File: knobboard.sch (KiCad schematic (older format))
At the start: 0 parts

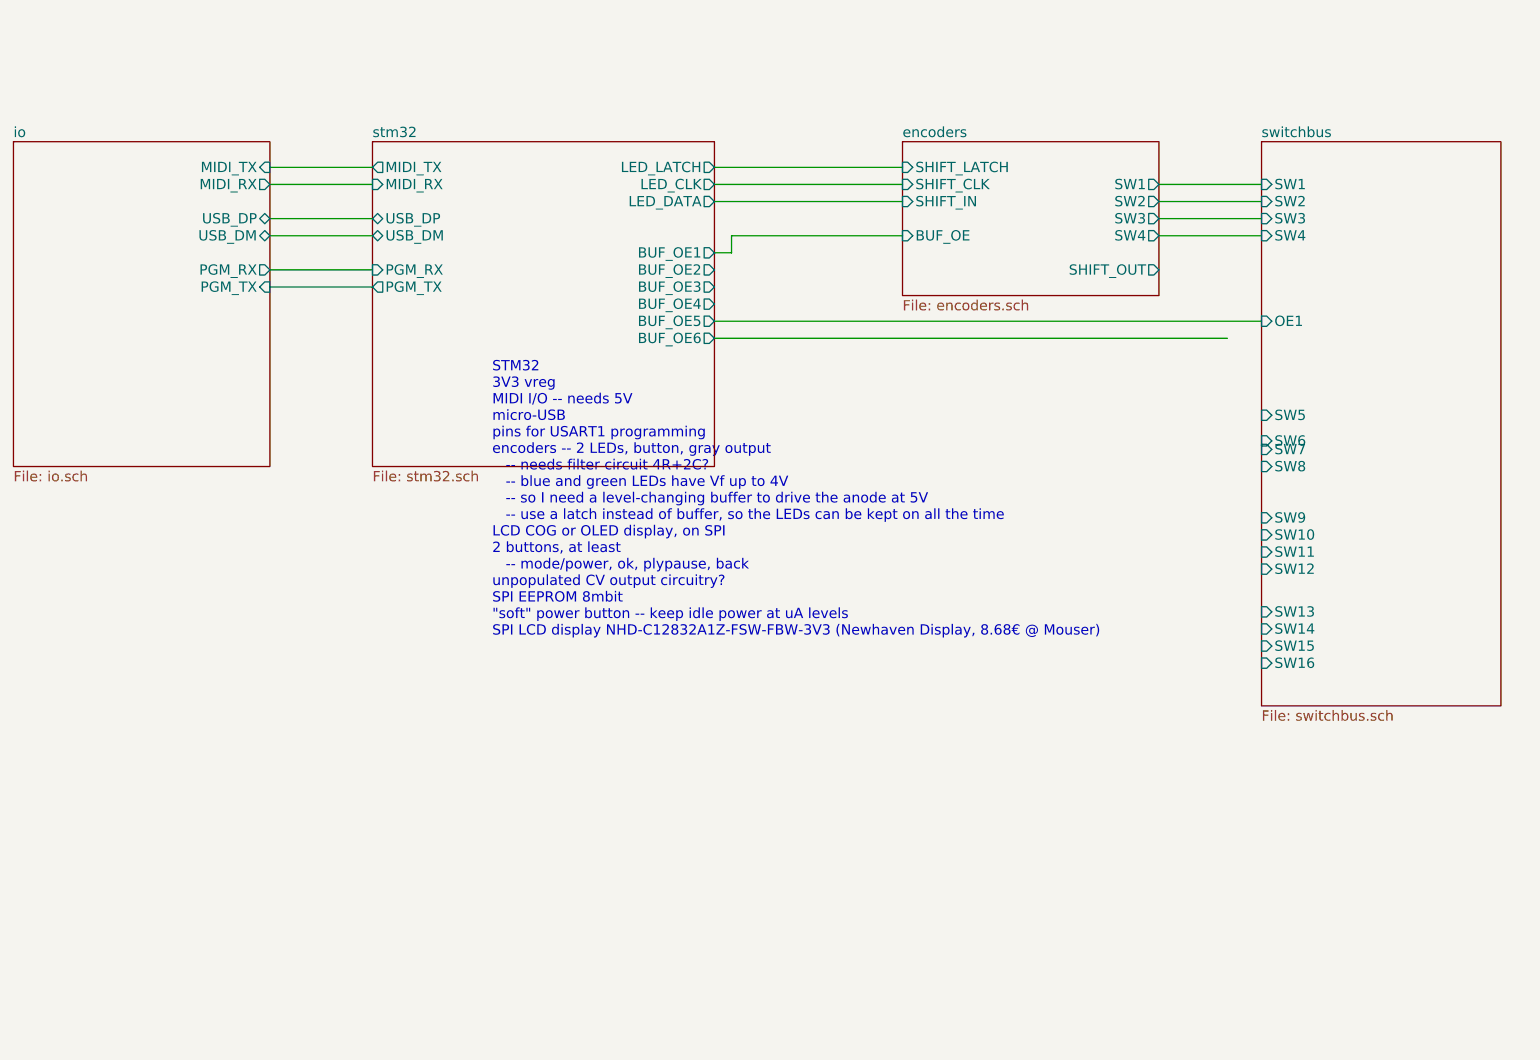
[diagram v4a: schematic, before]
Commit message: Switch to shift registers. Routing.
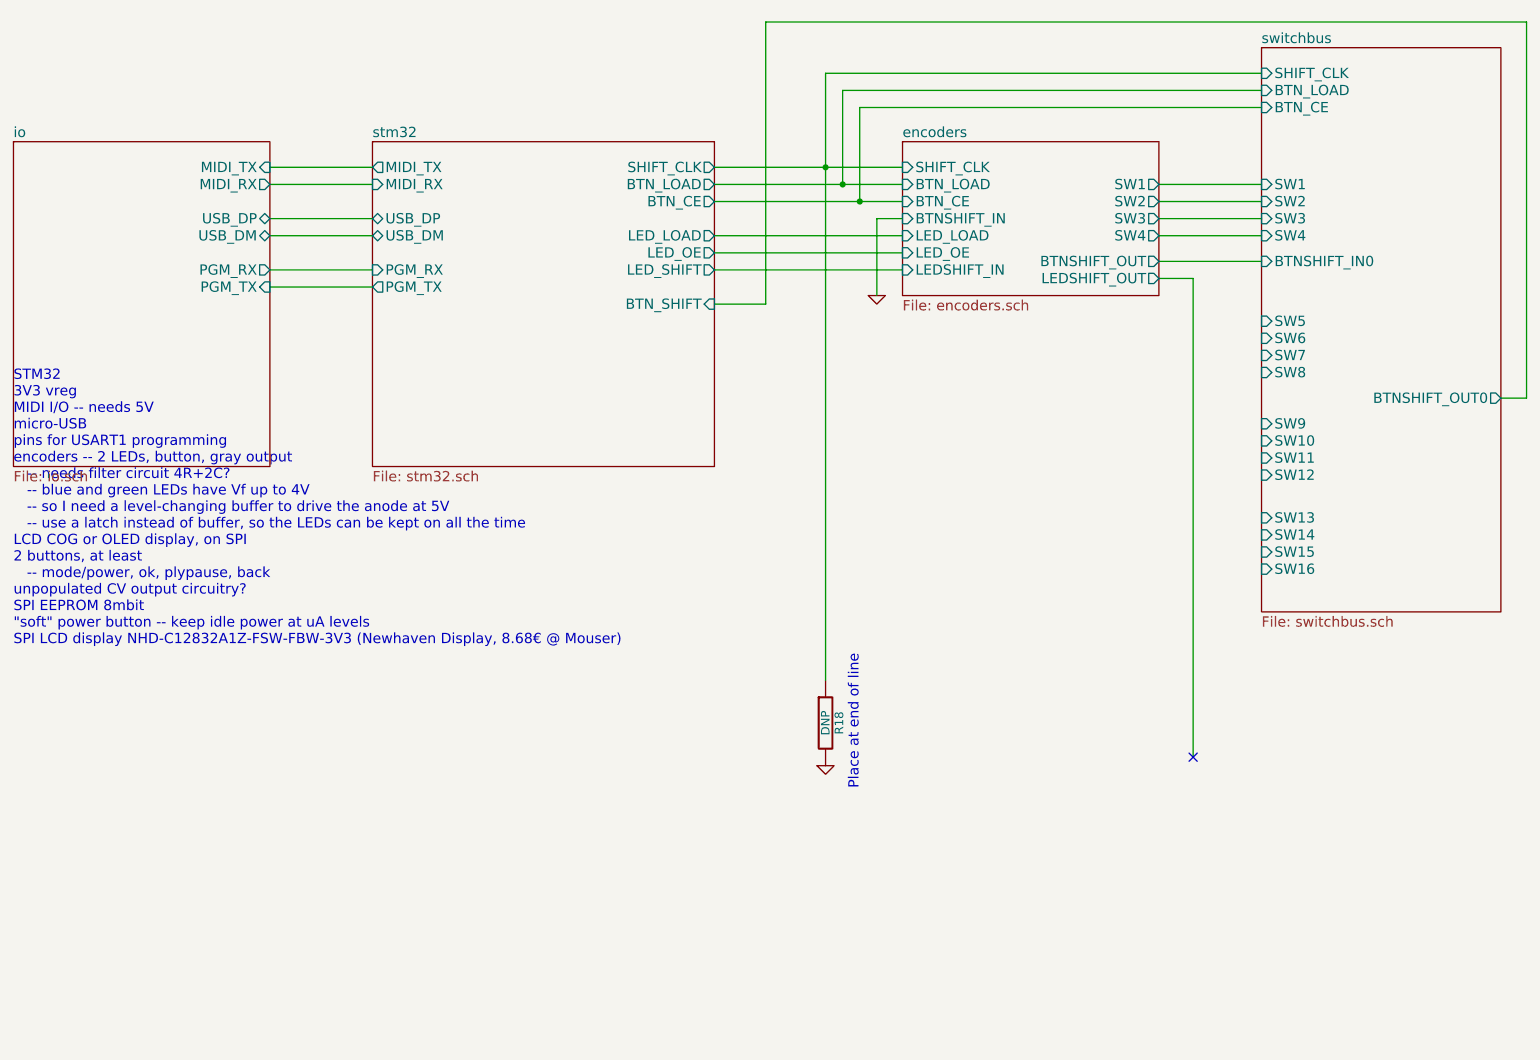
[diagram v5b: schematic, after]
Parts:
- added R18: DNP, symbol R
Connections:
- net labels added: GND
- wire segments 18 -> 32
- no-connect marks 0 -> 1
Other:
- note added: "Place at end of line"
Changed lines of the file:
@@
-EESchema Schematic File Version 2  date Sun 15 Apr 2012 10:50:25 AM CEST
+EESchema Schematic File Version 2  date Tue 17 Apr 2012 08:42:54 PM CEST
 LIBS:power
 LIBS:device
@@
 Sheet 1 5
 Title ""
-Date "15 apr 2012"
+Date "17 apr 2012"
 Rev ""
 Comp ""
@@
 $EndDescr
 Wire Wire Line
-	8800 2600 5600 2600
+	5600 2500 5900 2500
+Wire Wire Line
+	5900 2500 5900 850
+Wire Wire Line
+	5900 850  10350 850
+Wire Wire Line
+	10350 850  10350 3050
+Wire Wire Line
+	10350 3050 10200 3050
+Connection ~ 6450 1900
+Wire Wire Line
+	6450 1900 6450 1350
+Wire Wire Line
+	6450 1350 8800 1350
+Wire Wire Line
+	6250 4700 6250 1150
+Wire Wire Line
+	6250 1150 8800 1150
+Wire Wire Line
+	6550 2450 6550 2000
+Wire Wire Line
+	6550 2000 6700 2000
+Wire Wire Line
+	5600 2200 6700 2200
+Wire Wire Line
+	5600 1900 6700 1900
+Wire Wire Line
+	5600 1700 6700 1700
 Wire Wire Line
 	8200 1900 8800 1900
@@
 	3000 1700 3600 1700
 Wire Wire Line
-	5600 1900 6700 1900
-Wire Wire Line
-	5600 1700 6700 1700
-Wire Wire Line
-	5600 1800 6700 1800
-Wire Wire Line
-	5600 2200 5700 2200
-Wire Wire Line
-	5700 2200 5700 2100
-Wire Wire Line
-	5700 2100 6700 2100
-Wire Wire Line
 	3600 1800 3000 1800
 Wire Wire Line
@@
 	3600 2400 3000 2400
 Wire Wire Line
-	5600 2700 8600 2700
-Wire Wire Line
 	8200 2000 8800 2000
 Wire Wire Line
 	8200 1800 8800 1800
-$Sheet
-S 8800 1550 1400 3300
+Wire Wire Line
+	6700 2300 5600 2300
+Wire Wire Line
+	6700 1800 5600 1800
+Wire Wire Line
+	6700 2100 5600 2100
+Connection ~ 6250 1700
+Wire Wire Line
+	8200 2250 8800 2250
+Wire Wire Line
+	8800 1250 6350 1250
+Wire Wire Line
+	6350 1250 6350 1800
+Connection ~ 6350 1800
+Wire Wire Line
+	8200 2350 8400 2350
+Wire Wire Line
+	8400 2350 8400 5150
+NoConn ~ 8400 5150
+$Sheet
+S 8800 1000 1400 3300
 U 4F81A858
 F0 "switchbus" 60
 F1 "switchbus.sch" 60
-F2 "OE1" I L 8800 2600 60
-F3 "SW16" I L 8800 4600 60
-F4 "SW15" I L 8800 4500 60
-F5 "SW14" I L 8800 4400 60
-F6 "SW13" I L 8800 4300 60
-F7 "SW12" I L 8800 4050 60
-F8 "SW11" I L 8800 3950 60
-F9 "SW10" I L 8800 3850 60
-F10 "SW9" I L 8800 3750 60
-F11 "SW8" I L 8800 3450 60
-F12 "SW7" I L 8800 3350 60
-F13 "SW6" I L 8800 3300 60
-F14 "SW5" I L 8800 3150 60
-F15 "SW4" I L 8800 2100 60
-F16 "SW3" I L 8800 2000 60
-F17 "SW2" I L 8800 1900 60
-F18 "SW1" I L 8800 1800 60
+F2 "SW16" I L 8800 4050 60
+F3 "SW15" I L 8800 3950 60
+F4 "SW14" I L 8800 3850 60
+F5 "SW13" I L 8800 3750 60
+F6 "SW12" I L 8800 3500 60
+F7 "SW11" I L 8800 3400 60
+F8 "SW10" I L 8800 3300 60
+F9 "SW9" I L 8800 3200 60
+F10 "SW8" I L 8800 2900 60
+F11 "SW7" I L 8800 2800 60
+F12 "SW6" I L 8800 2700 60
+F13 "SW5" I L 8800 2600 60
+F14 "SW4" I L 8800 2100 60
+F15 "SW3" I L 8800 2000 60
+F16 "SW2" I L 8800 1900 60
+F17 "SW1" I L 8800 1800 60
+F18 "BTNSHIFT_OUT0" O R 10200 3050 60
+F19 "BTN_CE" I L 8800 1350 60
+F20 "BTN_LOAD" I L 8800 1250 60
+F21 "SHIFT_CLK" I L 8800 1150 60
+F22 "BTNSHIFT_IN0" I L 8800 2250 60
+$EndSheet
+$Comp
+L GND #PWR01
+U 1 1 4F8DA5D4
+P 6550 2450
+F 0 "#PWR01" H 6550 2450 30  0001 C CNN
+F 1 "GND" H 6550 2380 30  0001 C CNN
+	1    6550 2450
+	1    0    0    -1
+$EndComp
+Text Notes 6450 4550 3    60   ~ 0
+Place at end of line
+$Comp
+L GND #PWR02
+U 1 1 4F8DA3E0
+P 6250 5200
+F 0 "#PWR02" H 6250 5200 30  0001 C CNN
+F 1 "GND" H 6250 5130 30  0001 C CNN
+	1    6250 5200
+	1    0    0    -1
+$EndComp
+$Comp
+L R R18
+U 1 1 4F8DA3D4
+P 6250 4950
+F 0 "R18" V 6330 4950 50  0000 C CNN
+F 1 "DNP" V 6250 4950 50  0000 C CNN
+	1    6250 4950
+	1    0    0    -1
+$EndComp
+$Sheet
+S 6700 1550 1500 900
+U 4F7E05A5
+F0 "encoders" 60
+F1 "encoders.sch" 60
+F2 "SW4" O R 8200 2100 60
+F3 "SW3" O R 8200 2000 60
+F4 "SW2" O R 8200 1900 60
+F5 "SW1" O R 8200 1800 60
+F6 "SHIFT_CLK" I L 6700 1700 60
+F7 "BTN_LOAD" I L 6700 1800 60
+F8 "BTN_CE" I L 6700 1900 60
+F9 "BTNSHIFT_OUT" O R 8200 2250 60
+F10 "BTNSHIFT_IN" I L 6700 2000 60
+F11 "LEDSHIFT_OUT" O R 8200 2350 60
+F12 "LED_OE" I L 6700 2200 60
+F13 "LED_LOAD" I L 6700 2100 60
+F14 "LEDSHIFT_IN" I L 6700 2300 60
 $EndSheet
 $Sheet
@@
 F0 "stm32" 60
 F1 "stm32.sch" 60
-F2 "LED_LATCH" O R 5600 1700 60
-F3 "LED_DATA" O R 5600 1900 60
-F4 "LED_CLK" O R 5600 1800 60
-F5 "BUF_OE6" O R 5600 2700 60
-F6 "BUF_OE5" O R 5600 2600 60
-F7 "BUF_OE4" O R 5600 2500 60
-F8 "BUF_OE3" O R 5600 2400 60
-F9 "BUF_OE2" O R 5600 2300 60
-F10 "BUF_OE1" O R 5600 2200 60
-F11 "MIDI_TX" O L 3600 1700 60
-F12 "MIDI_RX" I L 3600 1800 60
-F13 "USB_DP" B L 3600 2000 60
-F14 "USB_DM" B L 3600 2100 60
-F15 "PGM_RX" I L 3600 2300 60
-F16 "PGM_TX" O L 3600 2400 60
-$EndSheet
-$Sheet
-S 6700 1550 1500 900
-U 4F7E05A5
-F0 "encoders" 60
-F1 "encoders.sch" 60
-F2 "BUF_OE" I L 6700 2100 60
-F3 "SW4" O R 8200 2100 60
-F4 "SW3" O R 8200 2000 60
-F5 "SW2" O R 8200 1900 60
-F6 "SW1" O R 8200 1800 60
-F7 "SHIFT_LATCH" I L 6700 1700 60
-F8 "SHIFT_CLK" I L 6700 1800 60
-F9 "SHIFT_OUT" O R 8200 2300 60
-F10 "SHIFT_IN" I L 6700 1900 60
-$EndSheet
-Text Notes 4300 4450 0    60   ~ 0
+F2 "MIDI_TX" O L 3600 1700 60
+F3 "MIDI_RX" I L 3600 1800 60
+F4 "USB_DP" B L 3600 2000 60
+F5 "USB_DM" B L 3600 2100 60
+F6 "PGM_RX" I L 3600 2300 60
+F7 "PGM_TX" O L 3600 2400 60
+F8 "LED_SHIFT" O R 5600 2300 60
+F9 "LED_OE" O R 5600 2200 60
+F10 "LED_LOAD" O R 5600 2100 60
+F11 "BTN_CE" O R 5600 1900 60
+F12 "BTN_LOAD" O R 5600 1800 60
+F13 "BTN_SHIFT" I R 5600 2500 60
+F14 "SHIFT_CLK" O R 5600 1700 60
+$EndSheet
+Text Notes 1500 4500 0    60   ~ 0
 STM32\n3V3 vreg\nMIDI I/O -- needs 5V\nmicro-USB\npins for USART1 programming\nencoders -- 2 LEDs, button, gray output\n   -- needs filter circuit 4R+2C?\n   -- blue and green LEDs have Vf up to 4V\n   -- so I need a level-changing buffer to drive the anode at 5V\n   -- use a latch instead of buffer, so the LEDs can be kept on all the time\nLCD COG or OLED display, on SPI\n2 buttons, at least\n   -- mode/power, ok, plypause, back\nunpopulated CV output circuitry?\nSPI EEPROM 8mbit\n"soft" power button -- keep idle power at uA levels\nSPI LCD display NHD-C12832A1Z-FSW-FBW-3V3 (Newhaven Display, 8.68€ @ Mouser)
 $EndSCHEMATC

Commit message: Routing
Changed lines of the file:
@@
-EESchema Schematic File Version 2  date Tue 17 Apr 2012 08:42:54 PM CEST
+EESchema Schematic File Version 2  date Thu 19 Apr 2012 08:23:14 PM CEST
 LIBS:power
 LIBS:device
@@
 Sheet 1 5
 Title ""
-Date "17 apr 2012"
+Date "19 apr 2012"
 Rev ""
 Comp ""
@@
 $EndDescr
 Wire Wire Line
-	5600 2500 5900 2500
+	6700 2000 6150 2000
 Wire Wire Line
-	5900 2500 5900 850
+	6150 2000 6150 800
 Wire Wire Line
-	5900 850  10350 850
+	6150 800  10350 800
 Wire Wire Line
-	10350 850  10350 3050
+	10350 800  10350 3050
 Wire Wire Line
-	10350 3050 10200 3050
-Connection ~ 6450 1900
+	5900 2650 5900 2500
 Wire Wire Line
-	6450 1900 6450 1350
+	5900 2650 8600 2650
 Wire Wire Line
-	6450 1350 8800 1350
+	8600 2650 8600 2250
 Wire Wire Line
-	6250 4700 6250 1150
+	8600 2250 8200 2250
 Wire Wire Line
-	6250 1150 8800 1150
+	8200 2350 8400 2350
+Connection ~ 6350 1800
 Wire Wire Line
-	6550 2450 6550 2000
+	6350 1800 6350 1250
 Wire Wire Line
-	6550 2000 6700 2000
+	6350 1250 8800 1250
+Connection ~ 6250 1700
+Wire Wire Line
+	6700 2100 5600 2100
+Wire Wire Line
+	6700 1800 5600 1800
+Wire Wire Line
+	6700 2300 5600 2300
+Wire Wire Line
+	8200 1800 8800 1800
+Wire Wire Line
+	8200 2000 8800 2000
+Wire Wire Line
+	3600 2400 3000 2400
+Wire Wire Line
+	3600 2100 3000 2100
+Wire Wire Line
+	3600 1800 3000 1800
+Wire Wire Line
+	3000 1700 3600 1700
+Wire Wire Line
+	3000 2000 3600 2000
+Wire Wire Line
+	3000 2300 3600 2300
+Wire Wire Line
+	8200 2100 8800 2100
+Wire Wire Line
+	8200 1900 8800 1900
+Wire Wire Line
+	5600 1700 6700 1700
+Wire Wire Line
+	5600 1900 6700 1900
 Wire Wire Line
 	5600 2200 6700 2200
 Wire Wire Line
-	5600 1900 6700 1900
+	8800 1150 6250 1150
 Wire Wire Line
-	5600 1700 6700 1700
+	6250 1150 6250 4700
 Wire Wire Line
-	8200 1900 8800 1900
+	8800 1350 6450 1350
 Wire Wire Line
-	8200 2100 8800 2100
+	6450 1350 6450 1900
+Connection ~ 6450 1900
 Wire Wire Line
-	3000 2300 3600 2300
+	10350 3050 10200 3050
 Wire Wire Line
-	3000 2000 3600 2000
-Wire Wire Line
-	3000 1700 3600 1700
-Wire Wire Line
-	3600 1800 3000 1800
-Wire Wire Line
-	3600 2100 3000 2100
-Wire Wire Line
-	3600 2400 3000 2400
-Wire Wire Line
-	8200 2000 8800 2000
-Wire Wire Line
-	8200 1800 8800 1800
-Wire Wire Line
-	6700 2300 5600 2300
-Wire Wire Line
-	6700 1800 5600 1800
-Wire Wire Line
-	6700 2100 5600 2100
-Connection ~ 6250 1700
-Wire Wire Line
-	8200 2250 8800 2250
-Wire Wire Line
-	8800 1250 6350 1250
-Wire Wire Line
-	6350 1250 6350 1800
-Connection ~ 6350 1800
-Wire Wire Line
-	8200 2350 8400 2350
+	5900 2500 5600 2500
 Wire Wire Line
 	8400 2350 8400 5150
@@
 L GND #PWR01
 U 1 1 4F8DA5D4
-P 6550 2450
-F 0 "#PWR01" H 6550 2450 30  0001 C CNN
-F 1 "GND" H 6550 2380 30  0001 C CNN
-	1    6550 2450
+P 7550 4250
+F 0 "#PWR01" H 7550 4250 30  0001 C CNN
+F 1 "GND" H 7550 4180 30  0001 C CNN
+	1    7550 4250
 	1    0    0    -1
 $EndComp

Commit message: Routing
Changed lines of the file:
@@
-EESchema Schematic File Version 2  date Thu 19 Apr 2012 08:23:14 PM CEST
+EESchema Schematic File Version 2  date Thu 19 Apr 2012 10:08:52 PM CEST
 LIBS:power
 LIBS:device
@@
 $Descr A4 11700 8267
 encoding utf-8
-Sheet 1 5
+Sheet 1 6
 Title ""
 Date "19 apr 2012"
@@
 Comment4 ""
 $EndDescr
+Connection ~ 6050 2200
+Wire Wire Line
+	6050 2200 6050 3400
+Wire Wire Line
+	6050 3400 6700 3400
+Wire Wire Line
+	6450 3100 6450 1350
+Wire Wire Line
+	6450 3100 6700 3100
+Connection ~ 6250 2900
+Wire Wire Line
+	6700 2900 6250 2900
+Wire Wire Line
+	6700 3500 6550 3500
+Wire Wire Line
+	6550 3500 6550 2650
+Wire Wire Line
+	6550 2650 8500 2650
+Wire Wire Line
+	8500 2650 8500 2350
+Wire Wire Line
+	8500 2350 8200 2350
+Wire Wire Line
+	8800 3200 8200 3200
+Wire Wire Line
+	8800 3000 8200 3000
 Wire Wire Line
 	6700 2000 6150 2000
@@
 	10350 800  10350 3050
 Wire Wire Line
-	5900 2650 5900 2500
-Wire Wire Line
-	5900 2650 8600 2650
-Wire Wire Line
-	8600 2650 8600 2250
+	5900 2550 5900 2500
+Wire Wire Line
+	5900 2550 8600 2550
+Wire Wire Line
+	8600 2550 8600 2250
 Wire Wire Line
 	8600 2250 8200 2250
-Wire Wire Line
-	8200 2350 8400 2350
 Connection ~ 6350 1800
 Wire Wire Line
-	6350 1800 6350 1250
-Wire Wire Line
-	6350 1250 8800 1250
+	8800 1250 6350 1250
 Connection ~ 6250 1700
 Wire Wire Line
@@
 	6250 1150 6250 4700
 Wire Wire Line
-	8800 1350 6450 1350
-Wire Wire Line
-	6450 1350 6450 1900
+	6450 1350 8800 1350
 Connection ~ 6450 1900
 Wire Wire Line
@@
 	5900 2500 5600 2500
 Wire Wire Line
-	8400 2350 8400 5150
+	8200 2900 8800 2900
+Wire Wire Line
+	8200 3100 8800 3100
+Wire Wire Line
+	8200 3450 8800 3450
+Wire Wire Line
+	8200 3550 8400 3550
+Wire Wire Line
+	8400 3550 8400 5150
+Wire Wire Line
+	6700 3000 6350 3000
+Wire Wire Line
+	6350 3000 6350 1250
+Wire Wire Line
+	6700 3300 6150 3300
+Wire Wire Line
+	6150 3300 6150 2100
+Connection ~ 6150 2100
+$Sheet
+S 6700 2750 1500 900
+U 4F905A24
+F0 "encoders2" 60
+F1 "encoders2.sch" 60
+F2 "SHIFT_CLK" I L 6700 2900 60
+F3 "BTN_LOAD" I L 6700 3000 60
+F4 "BTN_CE" I L 6700 3100 60
+F5 "BTNSHIFT_OUT" O R 8200 3450 60
+F6 "BTNSHIFT_IN" I L 6700 3200 60
+F7 "LEDSHIFT_OUT" O R 8200 3550 60
+F8 "LED_OE" I L 6700 3400 60
+F9 "LED_LOAD" I L 6700 3300 60
+F10 "LEDSHIFT_IN" I L 6700 3500 60
+F11 "SW4" O R 8200 3200 60
+F12 "SW3" O R 8200 3100 60
+F13 "SW2" O R 8200 3000 60
+F14 "SW1" O R 8200 2900 60
+$EndSheet
 NoConn ~ 8400 5150
 $Sheet
-S 8800 1000 1400 3300
+S 8800 1000 1400 4900
 U 4F81A858
 F0 "switchbus" 60
 F1 "switchbus.sch" 60
-F2 "SW16" I L 8800 4050 60
-F3 "SW15" I L 8800 3950 60
-F4 "SW14" I L 8800 3850 60
-F5 "SW13" I L 8800 3750 60
-F6 "SW12" I L 8800 3500 60
-F7 "SW11" I L 8800 3400 60
-F8 "SW10" I L 8800 3300 60
-F9 "SW9" I L 8800 3200 60
-F10 "SW8" I L 8800 2900 60
-F11 "SW7" I L 8800 2800 60
-F12 "SW6" I L 8800 2700 60
-F13 "SW5" I L 8800 2600 60
+F2 "SW16" I L 8800 4600 60
+F3 "SW15" I L 8800 4500 60
+F4 "SW14" I L 8800 4400 60
+F5 "SW13" I L 8800 4300 60
+F6 "SW12" I L 8800 4150 60
+F7 "SW11" I L 8800 4050 60
+F8 "SW10" I L 8800 3950 60
+F9 "SW9" I L 8800 3850 60
+F10 "SW8" I L 8800 3200 60
+F11 "SW7" I L 8800 3100 60
+F12 "SW6" I L 8800 3000 60
+F13 "SW5" I L 8800 2900 60
 F14 "SW4" I L 8800 2100 60
 F15 "SW3" I L 8800 2000 60
@@
 F20 "BTN_LOAD" I L 8800 1250 60
 F21 "SHIFT_CLK" I L 8800 1150 60
-F22 "BTNSHIFT_IN0" I L 8800 2250 60
+F22 "BTNSHIFT_IN0" I L 8800 3450 60
 $EndSheet
 $Comp
 L GND #PWR01
 U 1 1 4F8DA5D4
-P 7550 4250
-F 0 "#PWR01" H 7550 4250 30  0001 C CNN
-F 1 "GND" H 7550 4180 30  0001 C CNN
-	1    7550 4250
+P 6500 5800
+F 0 "#PWR01" H 6500 5800 30  0001 C CNN
+F 1 "GND" H 6500 5730 30  0001 C CNN
+	1    6500 5800
 	1    0    0    -1
 $EndComp
